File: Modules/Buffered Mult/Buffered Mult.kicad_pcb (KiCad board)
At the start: 2 copper layers, 50 x 200 mm, 20 parts

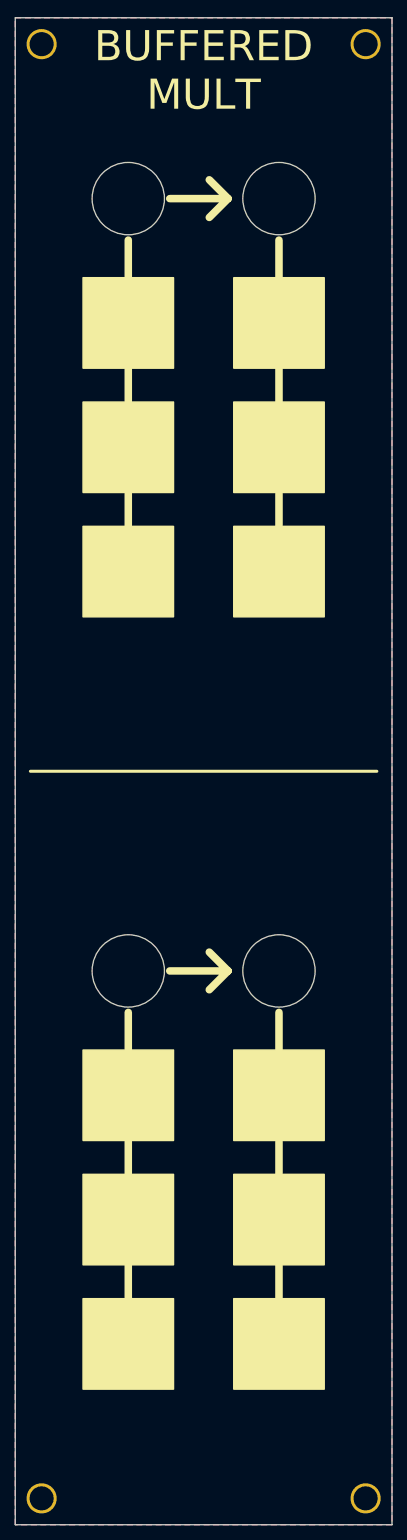
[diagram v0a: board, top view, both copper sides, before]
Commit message: Updated jack types and decals
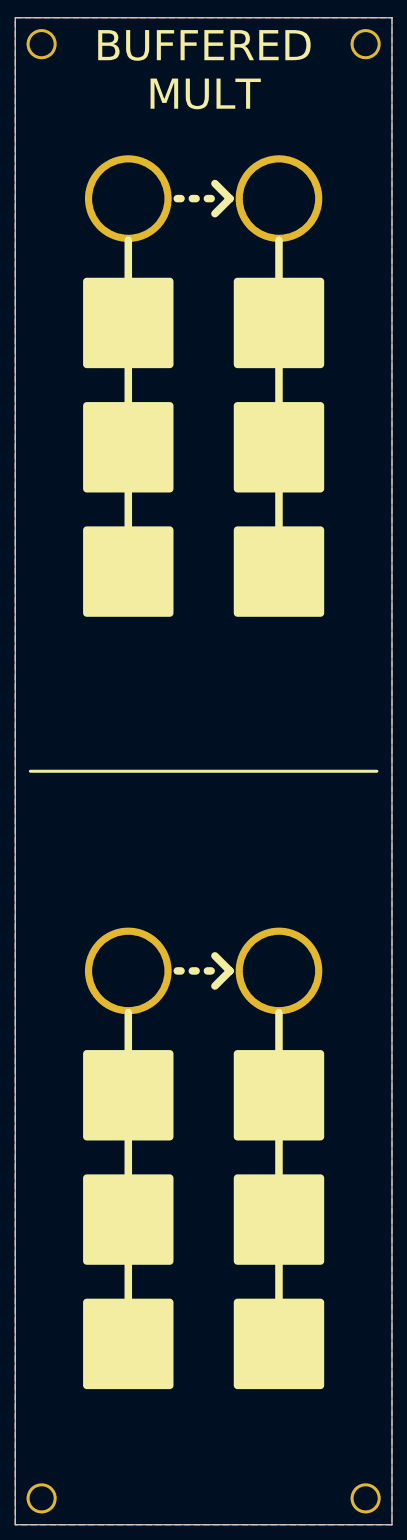
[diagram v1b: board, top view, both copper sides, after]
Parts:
- H10, H11, H12, H15, H16, H17, H18, H19, H20, H7, H8, H9: value MountingHole_Jack6.35mm -> Output; footprint SynthStuff:Jack_6.35mm_Cutout -> SynthStuff:Jack_6.35mm_Cutout_Output
- H13, H14, H5, H6: value MountingHole_Jack6.35mm -> Input

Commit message: Used jack holes with edge cuts
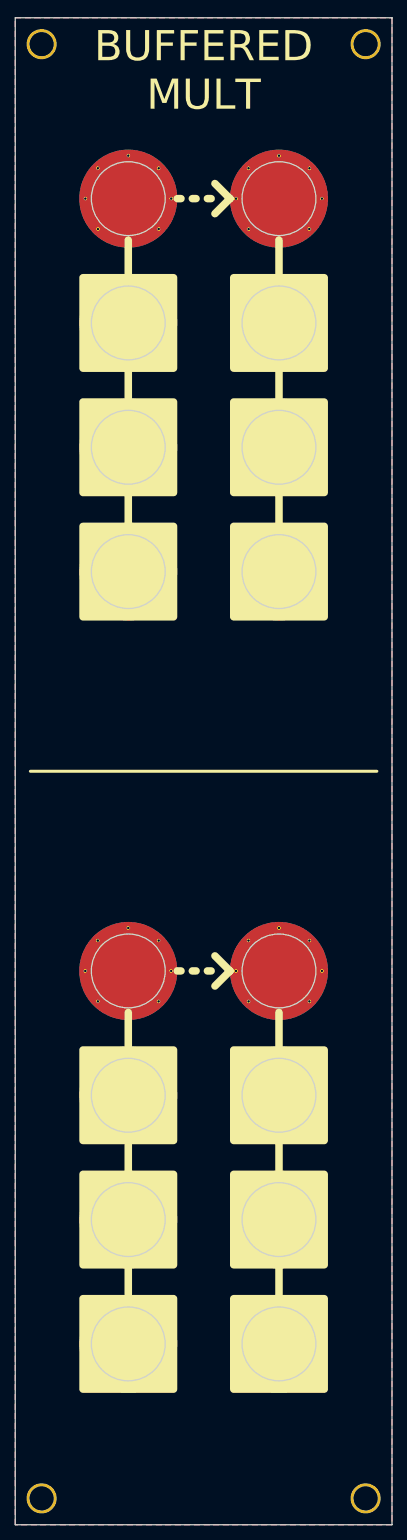
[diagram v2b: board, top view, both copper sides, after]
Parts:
- H10, H11, H12, H15, H16, H17, H18, H19, H20, H7, H8, H9: footprint SynthStuff:Jack_6.35mm_Cutout_Output -> SynthStuff:Jack_6.35mm_Cutout_Output_v2
- H13, H14, H5, H6: footprint SynthStuff:Jack_6.35mm_Cutout -> SynthStuff:Jack_6.35mm_Cutout_v2
